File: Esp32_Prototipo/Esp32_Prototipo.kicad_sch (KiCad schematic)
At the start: 18 parts, among them J1 Fan, J2 Screw_Terminal_01x04, J3 Screw_Terminal_01x04, J4 Input, Q1 2N7002K, U1 ESP32-DEVKITC-32D

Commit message: proto esp32 pronto para montar
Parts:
- added C1, C3: 100uF, Capacitor_THT:CP_Radial_D6.3mm_P2.50mm, symbol Device:C_Polarized_Small_US
- added C2: 220n, Capacitor_THT:C_Disc_D5.0mm_W2.5mm_P5.00mm, symbol Device:C
- added JP1: Jumper_3_Bridged12, Connector_PinHeader_2.54mm:PinHeader_1x03_P2.54mm_Vertical, symbol Jumper:Jumper_3_Bridged12
- added R1, R2, R3: 2k2, Resistor_THT:R_Axial_DIN0207_L6.3mm_D2.5mm_P10.16mm_Horizontal, symbol Device:R
- added U2: LM7805_TO220, Package_TO_SOT_THT:TO-220-3_Vertical, symbol Regulator_Linear:LM7805_TO220
- added U3: E32-433T20D, footprints6:E32-xxxT20D, symbol E32-xxxT20D:E32-433T20D
- renumbered C1 to C4, C2 to C5, J4 to J1, J1 to J2, J2 to J3, J3 to J4, R1 to R4, R2 to R5, R3 to R6, R4 to R7, R5 to R8, R6 to R9
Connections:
- net +3V3: now also R1.1, R2.1, R3.1
- net +BATT: now also C3.1, JP1.2 (C), U3.6 (VCC); no longer D1.1 (K)
- net GND: now also C1.2, C2.1, C3.2, U2.2 (GND), U3.7 (GND)
- net AUX: now reaches U1.J3-12 (IO16)
- net AUX: now also R1.2, U3.5 (AUX)
- net TXD: now reaches U1.J3-13 (IO4)
- net TXD: now also U3.4 (TXD)
- net RXD: now reaches U1.J3-14 (IO0)
- net RXD: now also U3.3 (RXD)
- net M1: now reaches U1.J3-15 (IO2)
- net M1: now also R2.2, U3.2 (M1)
- net M0: now reaches U1.J3-16 (IO15)
- net M0: now also R3.2, U3.1 (M0)
- new net: C1.1, D1.1 (K), JP1.3 (B), U2.1 (VI)
- new net: C2.2, JP1.1 (A), U2.3 (VO)
- no-connect marks 0 -> 26
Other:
- moved on the sheet: D1, J1, U1

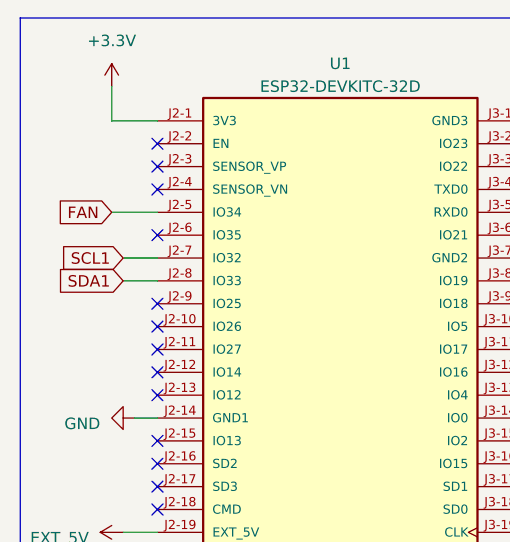
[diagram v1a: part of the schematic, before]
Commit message: corrigido falha no schematico e alargado as trilhas
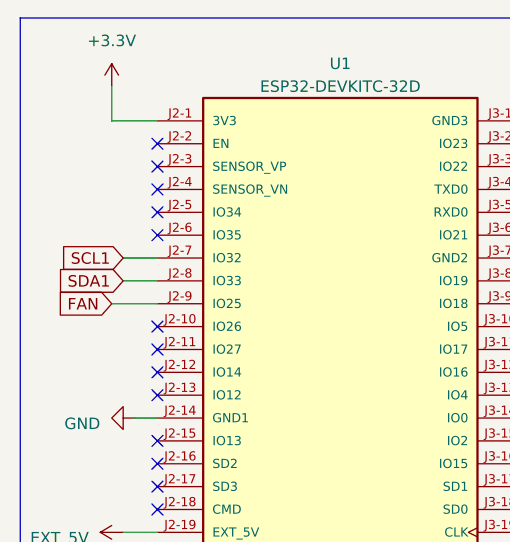
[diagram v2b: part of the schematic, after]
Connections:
- net FAN: now also U1.J2-9 (IO25); no longer U1.J2-5 (IO34)
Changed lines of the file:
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@@
   (no_connect (at 30.48 54.61))
   (no_connect (at 30.48 67.31))
+  (no_connect (at 30.48 36.83))
   (no_connect (at 71.12 49.53))
   (no_connect (at 71.12 46.99))
@@
   (no_connect (at 30.48 64.77))
   (no_connect (at 30.48 34.29))
-  (no_connect (at 30.48 46.99))
   (no_connect (at 71.12 69.85))
   (no_connect (at 30.48 52.07))
+  (wire (pts (xy 25.4 46.99) (xy 30.48 46.99))
+    (stroke (width 0) (type default))
+  )
   (wire (pts (xy 76.2 39.37) (xy 71.12 39.37))
     (stroke (width 0) (type default))
@@
   )
   (polyline (pts (xy 184.15 100.33) (xy 184.15 156.21))
-    (stroke (width 0) (type default))
-  )
-  (wire (pts (xy 25.4 36.83) (xy 30.48 36.83))
     (stroke (width 0) (type default))
   )
@@
     )
   )
-  (global_label "FAN" (shape input) (at 25.4 36.83 180) (fields_autoplaced)
-    (effects (font (size 1.27 1.27)) (justify right))
-    (property "Intersheetrefs" "${INTERSHEET_REFS}" (at -212.09 -78.74 0)
+  (global_label "FAN" (shape input) (at 25.4 46.99 180) (fields_autoplaced)
+    (effects (font (size 1.27 1.27)) (justify right))
+    (property "Intersheetrefs" "${INTERSHEET_REFS}" (at -212.09 -68.58 0)
       (effects (font (size 1.27 1.27)) hide)
     )
-    (property "Referências entre as folhas" "${INTERSHEET_REFS}" (at 19.4793 36.7506 0)
-      (effects (font (size 1.27 1.27)) (justify right) hide)
-    )
+    (property "Referências entre as folhas" "${INTERSHEET_REFS}" (at 19.4793 46.9106 0)
+      (effects (font (size 1.27 1.27)) (justify right) hide)
+    )
